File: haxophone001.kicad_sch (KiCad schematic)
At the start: 79 parts, among them J1 Conn_02x02_Odd_Even, J10 Conn_02x02_Odd_Even, J3 Raspberry_Pi_2_3, J4 Conn_01x03_Male, J5 Line Out, J6 Conn_02x02_Odd_Even, J8 Conn_02x02_Odd_Even, U1 MPXV7007DP, U2 MCP3221, U4 MAX98357

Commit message: Add external pull-up resistors to COL lines
The Raspberry Pi has 50k-60k internal pull-up resistors on GPIOs.  While this
is working correctly on a clean board, those values are a bit weak in the
presence of leakage paths which may appear in the presence of dirt and
humidity.  Increase the immunity to PCB leakage paths by adding lower
resistance (10k) external pull-up resistors.
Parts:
- added R3, R4, R5: 10K, Resistor_SMD:R_0805_2012Metric, symbol Device:R
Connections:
- net +3.3V: now also R3.1, R4.1, R5.1
- net COL0: now also R3.2
- net COL1: now also R4.2
- net COL2: now also R5.2
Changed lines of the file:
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@@
   (junction (at 245.11 90.17) (diameter 0) (color 0 0 0 0)
   )
+  (junction (at 186.69 25.4) (diameter 0) (color 0 0 0 0)
+  )
   (junction (at 104.14 64.77) (diameter 0) (color 0 0 0 0)
   )
@@
   (junction (at 83.82 125.73) (diameter 0) (color 0 0 0 0)
   )
+  (junction (at 166.37 25.4) (diameter 0) (color 0 0 0 0)
+  )
   (junction (at 143.51 110.49) (diameter 0) (color 0 0 0 0)
   )
@@
   (junction (at 186.69 93.98) (diameter 0) (color 0 0 0 0)
   )
+  (junction (at 143.51 25.4) (diameter 0) (color 0 0 0 0)
+  )
   (junction (at 237.49 90.17) (diameter 0) (color 0 0 0 0)
   )
@@
     (stroke (width 0) (type default))
   )
-  (wire (pts (xy 143.51 20.32) (xy 143.51 27.94))
-    (stroke (width 0) (type default))
-  )
   (wire (pts (xy 237.49 90.17) (xy 240.03 90.17))
     (stroke (width 0) (type default))
@@
     (stroke (width 0) (type default))
   )
-  (wire (pts (xy 166.37 20.32) (xy 166.37 27.94))
+  (wire (pts (xy 166.37 20.32) (xy 166.37 25.4))
     (stroke (width 0) (type default))
   )
@@
     (stroke (width 0) (type default))
   )
+  (wire (pts (xy 160.02 25.4) (xy 166.37 25.4))
+    (stroke (width 0) (type default))
+  )
   (wire (pts (xy 179.07 148.59) (xy 181.61 148.59))
     (stroke (width 0) (type default))
@@
     (stroke (width 0) (type default))
   )
-  (wire (pts (xy 186.69 20.32) (xy 186.69 93.98))
+  (wire (pts (xy 166.37 25.4) (xy 166.37 27.94))
+    (stroke (width 0) (type default))
+  )
+  (wire (pts (xy 180.34 25.4) (xy 186.69 25.4))
+    (stroke (width 0) (type default))
+  )
+  (wire (pts (xy 186.69 20.32) (xy 186.69 25.4))
     (stroke (width 0) (type default))
   )
@@
     (stroke (width 0) (type default))
   )
+  (wire (pts (xy 143.51 20.32) (xy 143.51 25.4))
+    (stroke (width 0) (type default))
+  )
   (wire (pts (xy 95.25 125.73) (xy 95.25 127))
     (stroke (width 0) (type default))
@@
     (stroke (width 0) (type default))
   )
+  (wire (pts (xy 186.69 25.4) (xy 186.69 93.98))
+    (stroke (width 0) (type default))
+  )
   (wire (pts (xy 77.47 58.42) (xy 74.93 58.42))
     (stroke (width 0) (type default))
   )
+  (wire (pts (xy 137.16 25.4) (xy 143.51 25.4))
+    (stroke (width 0) (type default))
+  )
   (wire (pts (xy 80.01 125.73) (xy 83.82 125.73))
     (stroke (width 0) (type default))
@@
     (stroke (width 0) (type default))
   )
+  (wire (pts (xy 143.51 25.4) (xy 143.51 27.94))
+    (stroke (width 0) (type default))
+  )
   (wire (pts (xy 166.37 77.47) (xy 166.37 60.96))
     (stroke (width 0) (type default))
@@
   (symbol (lib_id "MX_Alps_Hybrid:MX-NoLED") (at 162.56 29.21 0) (unit 1)
     (in_bom no) (on_board yes) (dnp no)
-    (property "Reference" "MX9" (at 163.3982 23.5458 0)
+    (property "Reference" "MX9" (at 156.21 29.21 0)
       (effects (font (size 1.524 1.524)))
     )
-    (property "Value" "f" (at 163.3982 25.4254 0)
+    (property "Value" "f" (at 158.75 26.67 0)
       (effects (font (size 0.508 0.508)))
     )
@@
   (symbol (lib_id "MX_Alps_Hybrid:MX-NoLED") (at 139.7 29.21 0) (unit 1)
     (in_bom no) (on_board yes) (dnp no)
-    (property "Reference" "MX8" (at 140.5382 23.5458 0)
+    (property "Reference" "MX8" (at 133.35 29.21 0)
       (effects (font (size 1.524 1.524)))
     )
-    (property "Value" "T" (at 140.5382 25.4254 0)
+    (property "Value" "T" (at 135.89 26.67 0)
       (effects (font (size 0.508 0.508)))
     )
@@
         )
       )
+    )
+  )
+  (symbol (lib_id "Device:R") (at 160.02 21.59 0) (unit 1)
+    (in_bom yes) (on_board yes) (dnp no)
+    (property "Reference" "R4" (at 156.21 20.32 0)
+      (effects (font (size 1.27 1.27)) (justify left))
+    )
+    (property "Value" "10K" (at 158.75 22.86 0)
+      (effects (font (size 1.27 1.27)) (justify right))
+    )
+    (property "Footprint" "Resistor_SMD:R_0805_2012Metric" (at 158.242 21.59 90)
+      (effects (font (size 1.27 1.27)) hide)
+    )
+    (property "Datasheet" "~" (at 160.02 21.59 0)
+      (effects (font (size 1.27 1.27)) hide)
+    )
+    (property "LCSC" "C17414" (at 160.02 21.59 0)
+      (effects (font (size 1.27 1.27)) hide)
+    )
+    (property "MPN" "0805W8F1002T5E" (at 160.02 21.59 0)
+      (effects (font (size 1.27 1.27)) hide)
+    )
+    (pin "1")
+    (pin "2")
+    (instances
+      (project "haxophone001"
+        (path "/227d5707-b625-491f-8a5f-be74f1284d6d"
+          (reference "R4") (unit 1)
+        )
+      )
+    )
+  )
+  (symbol (lib_id "power:+3.3V") (at 160.02 17.78 0) (unit 1)
+    (in_bom yes) (on_board yes) (dnp no)
+    (property "Reference" "#PWR017" (at 160.02 21.59 0)
+      (effects (font (size 1.27 1.27)) hide)
+    )
+    (property "Value" "+3.3V" (at 156.21 15.24 0)
+      (effects (font (size 1.27 1.27)))
+    )
+    (property "Footprint" "" (at 160.02 17.78 0)
+      (effects (font (size 1.27 1.27)) hide)
+    )
+    (property "Datasheet" "" (at 160.02 17.78 0)
+      (effects (font (size 1.27 1.27)) hide)
+    )
+    (pin "1")
+    (instances
+      (project "haxophone001"
+        (path "/227d5707-b625-491f-8a5f-be74f1284d6d"
+          (reference "#PWR017") (unit 1)
+        )
+      )
+    )
+  )
+  (symbol (lib_id "power:+3.3V") (at 180.34 17.78 0) (unit 1)
+    (in_bom yes) (on_board yes) (dnp no)
+    (property "Reference" "#PWR018" (at 180.34 21.59 0)
+      (effects (font (size 1.27 1.27)) hide)
+    )
+    (property "Value" "+3.3V" (at 176.53 15.24 0)
+      (effects (font (size 1.27 1.27)))
+    )
+    (property "Footprint" "" (at 180.34 17.78 0)
+      (effects (font (size 1.27 1.27)) hide)
+    )
+    (property "Datasheet" "" (at 180.34 17.78 0)
+      (effects (font (size 1.27 1.27)) hide)
+    )
+    (pin "1")
+    (instances
+      (project "haxophone001"
+        (path "/227d5707-b625-491f-8a5f-be74f1284d6d"
+          (reference "#PWR018") (unit 1)
+        )
+      )
+    )
+  )
+  (symbol (lib_id "Device:R") (at 137.16 21.59 0) (unit 1)
+    (in_bom yes) (on_board yes) (dnp no)
+    (property "Reference" "R3" (at 133.35 20.32 0)
+      (effects (font (size 1.27 1.27)) (justify left))
+    )
+    (property "Value" "10K" (at 135.89 22.86 0)
+      (effects (font (size 1.27 1.27)) (justify right))
+    )
+    (property "Footprint" "Resistor_SMD:R_0805_2012Metric" (at 135.382 21.59 90)
+      (effects (font (size 1.27 1.27)) hide)
+    )
+    (property "Datasheet" "~" (at 137.16 21.59 0)
+      (effects (font (size 1.27 1.27)) hide)
+    )
+    (property "LCSC" "C17414" (at 137.16 21.59 0)
+      (effects (font (size 1.27 1.27)) hide)
+    )
+    (property "MPN" "0805W8F1002T5E" (at 137.16 21.59 0)
+      (effects (font (size 1.27 1.27)) hide)
+    )
+    (pin "1")
+    (pin "2")
+    (instances
+      (project "haxophone001"
+        (path "/227d5707-b625-491f-8a5f-be74f1284d6d"
+          (reference "R3") (unit 1)
+        )
+      )
+    )
+  )
+  (symbol (lib_id "Device:R") (at 180.34 21.59 0) (unit 1)
+    (in_bom yes) (on_board yes) (dnp no)
+    (property "Reference" "R5" (at 176.53 20.32 0)
+      (effects (font (size 1.27 1.27)) (justify left))
+    )
+    (property "Value" "10K" (at 179.07 22.86 0)
+      (effects (font (size 1.27 1.27)) (justify right))
+    )
+    (property "Footprint" "Resistor_SMD:R_0805_2012Metric" (at 178.562 21.59 90)
+      (effects (font (size 1.27 1.27)) hide)
+    )
+    (property "Datasheet" "~" (at 180.34 21.59 0)
+      (effects (font (size 1.27 1.27)) hide)
+    )
+    (property "LCSC" "C17414" (at 180.34 21.59 0)
+      (effects (font (size 1.27 1.27)) hide)
+    )
+    (property "MPN" "0805W8F1002T5E" (at 180.34 21.59 0)
+      (effects (font (size 1.27 1.27)) hide)
+    )
+    (pin "1")
+    (pin "2")
+    (instances
+      (project "haxophone001"
+        (path "/227d5707-b625-491f-8a5f-be74f1284d6d"
+          (reference "R5") (unit 1)
+        )
+      )
+    )
+  )
+  (symbol (lib_id "power:+3.3V") (at 137.16 17.78 0) (unit 1)
+    (in_bom yes) (on_board yes) (dnp no)
+    (property "Reference" "#PWR07" (at 137.16 21.59 0)
+      (effects (font (size 1.27 1.27)) hide)
+    )
+    (property "Value" "+3.3V" (at 133.35 15.24 0)
+      (effects (font (size 1.27 1.27)))
+    )
+    (property "Footprint" "" (at 137.16 17.78 0)
+      (effects (font (size 1.27 1.27)) hide)
+    )
+    (property "Datasheet" "" (at 137.16 17.78 0)
+      (effects (font (size 1.27 1.27)) hide)
+    )
+    (pin "1")
+    (instances
+      (project "haxophone001"
+        (path "/227d5707-b625-491f-8a5f-be74f1284d6d"
+          (reference "#PWR07") (unit 1)
+        )
+      )

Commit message: Fix incorrect cap part 1uF -> 0.1uF
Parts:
- C2: LCSC C28323 -> C1525
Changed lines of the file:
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@@
       (effects (font (size 1.27 1.27)) hide)
     )
-    (property "LCSC" "C28323" (at 21.59 127 0)
+    (property "LCSC" "C1525" (at 21.59 127 0)
       (effects (font (size 1.27 1.27)) hide)
     )

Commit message: Fixup: Use the right foogprint for C2
The previous commit fixed the cap value, but introduced the wrong
capacitor size, 0402.  Correct this by selecting a 0603 cap for C2.
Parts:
- C2: LCSC C1525 -> C14663
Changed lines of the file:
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@@
       (effects (font (size 1.27 1.27)) hide)
     )
-    (property "LCSC" "C1525" (at 21.59 127 0)
+    (property "LCSC" "C14663" (at 21.59 127 0)
       (effects (font (size 1.27 1.27)) hide)
     )

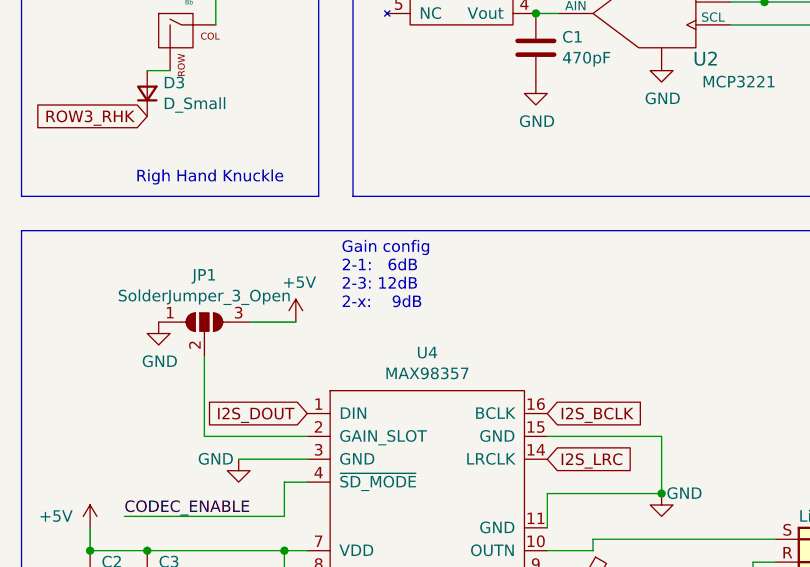
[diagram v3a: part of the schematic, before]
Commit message: Fix gain selection documentation label
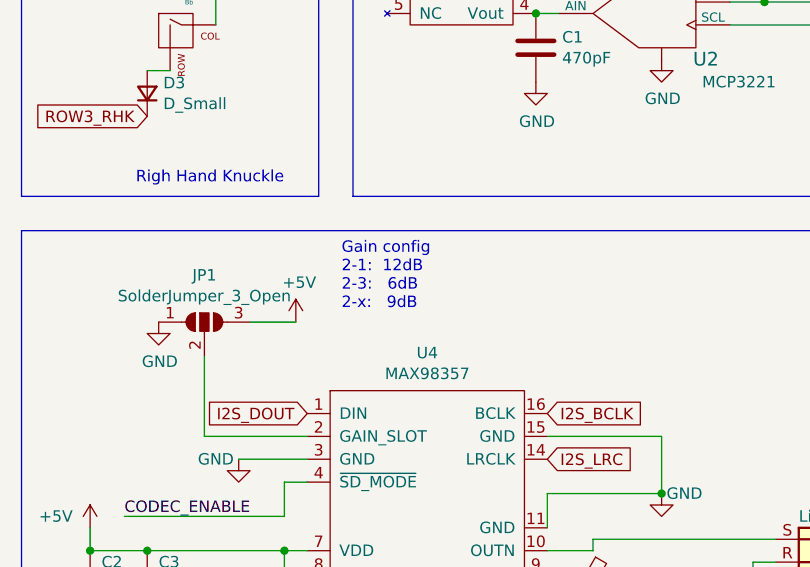
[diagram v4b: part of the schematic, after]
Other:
- note added: "Gain config 2-1: 12dB 2-3: 6dB 2-x: 9dB"
- note removed: "Gain config 2-1: 6dB 2-3: 12dB 2-x: 9dB"
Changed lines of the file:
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@@
     (effects (font (size 1.27 1.27)) (justify left bottom))
   )
-  (text "Gain config\n2-1:   6dB\n2-3: 12dB\n2-x:    9dB" (at 49.53 96.52 0)
+  (text "Gain config\n2-1:  12dB\n2-3:   6dB\n2-x:   9dB" (at 49.53 96.52 0)
     (effects (font (size 1.27 1.27)) (justify left bottom))
   )
